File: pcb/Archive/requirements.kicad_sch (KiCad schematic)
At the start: 0 parts

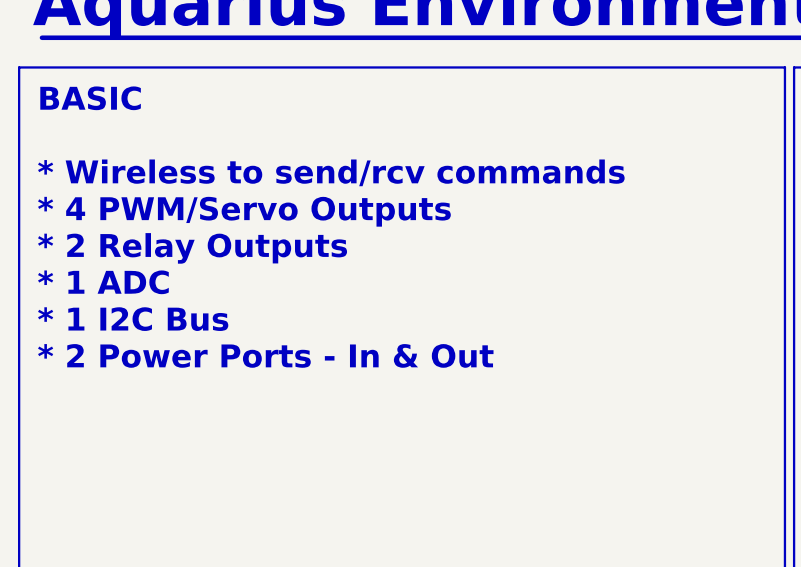
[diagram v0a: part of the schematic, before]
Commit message: Added interfaces and fully routed PCB
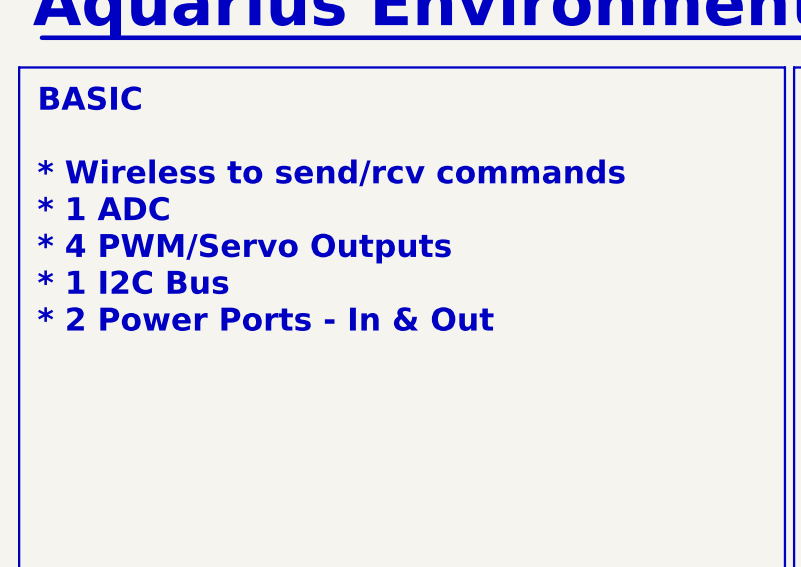
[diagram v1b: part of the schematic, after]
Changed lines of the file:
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@@
 		)
 	)
-	(text_box "BASIC\n\n* Wireless to send/rcv commands\n* 4 PWM/Servo Outputs\n* 2 Relay Outputs\n* 1 ADC\n* 1 I2C Bus\n* 2 Power Ports - In & Out"
+	(text_box "BASIC\n\n* Wireless to send/rcv commands\n* 1 ADC\n* 4 PWM/Servo Outputs\n* 1 I2C Bus\n* 2 Power Ports - In & Out\n"
 		(exclude_from_sim yes)
 		(at 17.78 30.48 0)
